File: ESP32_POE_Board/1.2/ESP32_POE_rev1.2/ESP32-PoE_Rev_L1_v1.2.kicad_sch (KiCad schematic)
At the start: 128 parts, among them Q1 Q12MHz/20pF/10ppm/4P/3.2x2.5mm, Q2 BC817-40(SOT23), Q3 BC817-40(SOT23), T1 LMUN2211LT1G(SOT-23), U1 CH340T(SSOP20W), U2 TPS2375D(SO-8), U3 BL4054B-42TPRN(SOT23-5), U4 LAN8710A-EZC(QFN32), U5 TX4138(ESOIC-8), U6 ESP32-WROVER-E, U7 SY8089AAAC(SOT23-5), U8 SN74LVC1G04DBVR(SOT23-5)

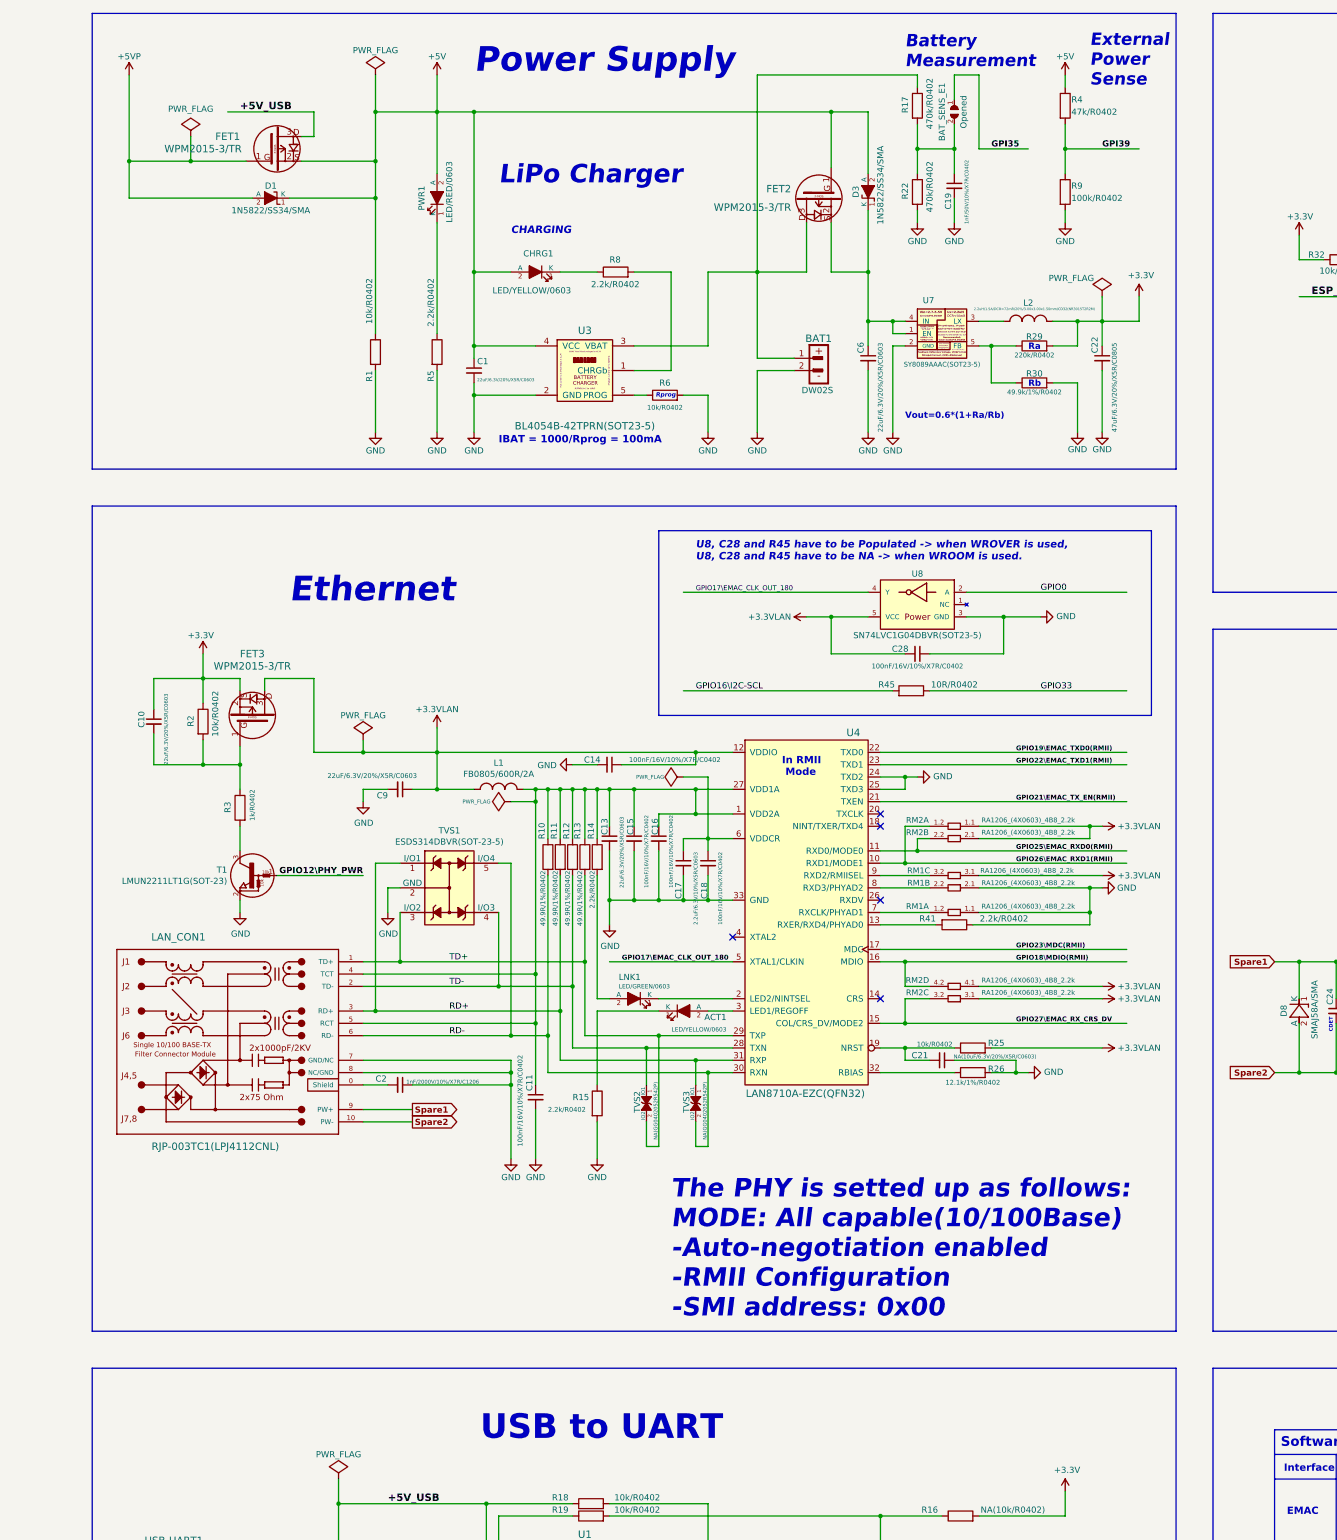
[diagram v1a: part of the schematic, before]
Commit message: new block diagrams
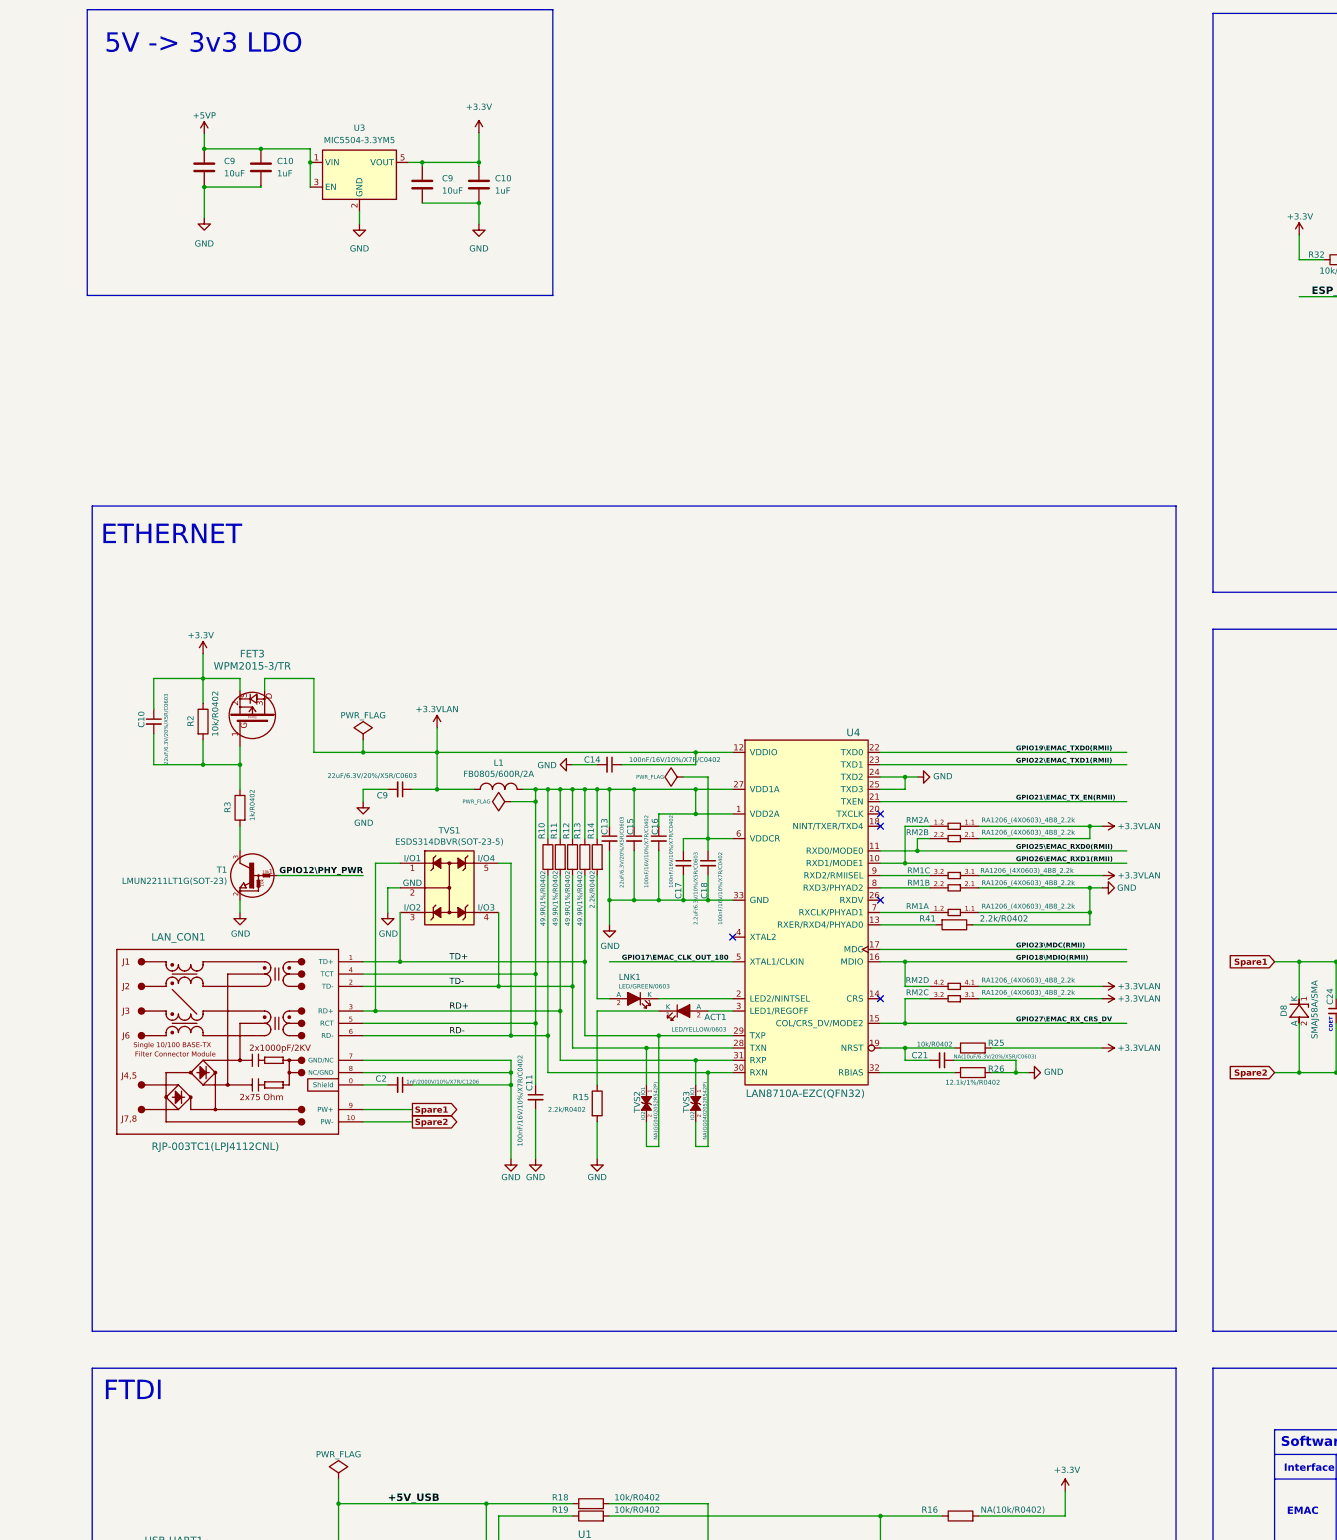
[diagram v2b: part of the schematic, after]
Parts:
- removed BAT1: DW02S, OLIMEX_Connectors-FP:LIPO_BAT_VERTICAL_DW02S, symbol ESP32-PoE_Rev_L1_v1.2-rescue:BAT_CON-ESP32-PoE_Rev_L1
- removed BAT_SENS_E1: Opened, OLIMEX_Jumpers-FP:SJ_1_SMALLER, symbol ESP32-PoE_Rev_L1_v1.2-rescue:SJ-ESP32-PoE_Rev_L1
- removed C1, C6: 22uF/6.3V/20%/X5R/C0603, OLIMEX_RLC-FP:C_0603_5MIL_DWS, symbol ESP32-PoE_Rev_L1_v1.2-rescue:C-ESP32-PoE_Rev_L1
- removed C19: 1nF/50V/10%/X7R/C0402, OLIMEX_RLC-FP:C_0402_5MIL_DWS, symbol ESP32-PoE_Rev_L1_v1.2-rescue:C-ESP32-PoE_Rev_L1
- removed C22: 47uF/6.3V/20%/X5R/C0805, OLIMEX_RLC-FP:C_0805_5MIL_DWS, symbol ESP32-PoE_Rev_L1_v1.2-rescue:C-ESP32-PoE_Rev_L1
- removed C28: 100nF/16V/10%/X7R/C0402, OLIMEX_RLC-FP:C_0402_5MIL_DWS, symbol ESP32-PoE_Rev_L1_v1.2-rescue:C-ESP32-PoE_Rev_L1
- removed CHRG1: LED/YELLOW/0603, OLIMEX_LEDs-FP:LED_0603_KA, symbol ESP32-PoE_Rev_L1_v1.2-rescue:LED-ESP32-PoE_Rev_L1
- removed D1, D3: 1N5822/SS34/SMA, OLIMEX_Diodes-FP:SMA-KA, symbol ESP32-PoE_Rev_L1_v1.2-rescue:D_Schottky-ESP32-PoE_Rev_L1
- removed FET1, FET2: WPM2015-3/TR, OLIMEX_Transistors-FP:SOT23, symbol ESP32-PoE_Rev_L1_v1.2-rescue:P-MOS+DIOD-ESP32-PoE_Rev_L1
- removed L2: 2.2uH/1.5A/DCR=72mR/20%/3.00x3.00x1.50mm/CD32(NR3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, OLIMEX_RLC-FP:CD32, symbol ESP32-PoE_Rev_L1_v1.2-rescue:L-ESP32-PoE_Rev_L1
- removed PWR1: LED/RED/0603, OLIMEX_LEDs-FP:LED_0603_KA, symbol ESP32-PoE_Rev_L1_v1.2-rescue:LED-ESP32-PoE_Rev_L1
- removed R1, R6: 10k/R0402, OLIMEX_RLC-FP:R_0402_5MIL_DWS, symbol ESP32-PoE_Rev_L1_v1.2-rescue:R-ESP32-PoE_Rev_L1
- removed R17, R22: 470k/R0402, OLIMEX_RLC-FP:R_0402_5MIL_DWS, symbol ESP32-PoE_Rev_L1_v1.2-rescue:R-ESP32-PoE_Rev_L1
- removed R29: 220k/R0402, OLIMEX_RLC-FP:R_0402_5MIL_DWS, symbol ESP32-PoE_Rev_L1_v1.2-rescue:R-ESP32-PoE_Rev_L1
- removed R30: 49.9k/1%/R0402, OLIMEX_RLC-FP:R_0402_5MIL_DWS, symbol ESP32-PoE_Rev_L1_v1.2-rescue:R-ESP32-PoE_Rev_L1
- removed R4: 47k/R0402, OLIMEX_RLC-FP:R_0402_5MIL_DWS, symbol ESP32-PoE_Rev_L1_v1.2-rescue:R-ESP32-PoE_Rev_L1
- removed R45: 10R/R0402, OLIMEX_RLC-FP:R_0402_5MIL_DWS, symbol ESP32-PoE_Rev_L1_v1.2-rescue:R-ESP32-PoE_Rev_L1
- removed R5, R8: 2.2k/R0402, OLIMEX_RLC-FP:R_0402_5MIL_DWS, symbol ESP32-PoE_Rev_L1_v1.2-rescue:R-ESP32-PoE_Rev_L1
- removed R9: 100k/R0402, OLIMEX_RLC-FP:R_0402_5MIL_DWS, symbol ESP32-PoE_Rev_L1_v1.2-rescue:R-ESP32-PoE_Rev_L1
- removed U3: BL4054B-42TPRN(SOT23-5), OLIMEX_IC-FP:SOT-23-5, symbol ESP32-PoE_Rev_L1_v1.2-rescue:BL4054B-42TPRN(SOT23-5)-ESP32-PoE_Rev_L1
- removed U7: SY8089AAAC(SOT23-5), OLIMEX_Regulators-FP:SOT-23-5, symbol ESP32-PoE_Rev_L1_v1.2-rescue:SY8009AAAC(SOT23-5)-ESP32-PoE_Rev_L1
- removed U8: SN74LVC1G04DBVR(SOT23-5), OLIMEX_IC-FP:SOT-23-5, symbol ESP32-PoE_Rev_L1_v1.2-rescue:SN74LVC1G04DBVR(SOT23-5)-ESP32-PoE_Rev_L1
- added C10 (x2): 1uF, Capacitor_SMD:C_0201_0603Metric, symbol Device:C
- added C9 (x2): 10uF, Capacitor_SMD:C_0603_1608Metric, symbol Device:C
- added U3: MIC5504-3.3YM5, Package_TO_SOT_SMD:SOT-23-5, symbol Regulator_Linear:MIC5504-3.3YM5
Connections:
- net +3.3V: now also C10.1, C9.1, U3.5 (VOUT)
- net +5VP: now also C10.1, C9.1, U3.1 (VIN), U3.3 (EN)
- net GND: now also C10.2, C10.2, C9.2, C9.2, U3.2 (GND)
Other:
- note added: "5V -> 3v3 LDO"
- note added: "ETHERNET"
- note added: "FTDI"
- note removed: "Battery Measurement"
- note removed: "CHARGING"
- note removed: "Ethernet"
- note removed: "External Power Sense"
- note removed: "IBAT = 1000/Rprog = 100mA"
- note removed: "In RMII Mode"
- note removed: "LiPo Charger"
- note removed: "Power Supply"
- note removed: "Rprog"
- note removed: "The PHY is setted up as follows: MODE: All capable(10/100Base) -Auto-negotiation enabled -RMII Configuration -SMI address: 0x00"
- note removed: "U8, C28 and R45 have to be Populated -> when WROVER is used, U8, C28 and R45 have to be NA -> when WROOM is used."
- note removed: "USB to UART"
- note removed: "Vout=0.6*(1+Ra/Rb)"

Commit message: fixing POE board symbols + circuit
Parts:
- removed C3: 47uF/6.3V/20%/X5R/C0805, OLIMEX_RLC-FP:C_0805_5MIL_DWS, symbol ESP32-PoE_Rev_L1_v1.2-rescue:C-ESP32-PoE_Rev_L1
- removed EXT1, EXT2: NS(HN1x10), OLIMEX_Connectors-FP:HN1x10, symbol ESP32-PoE_Rev_L1_v1.2-rescue:CON10-ESP32-PoE_Rev_L1
- removed L5: FB0805/600R/2A, OLIMEX_RLC-FP:L_0805_5MIL_DWS, symbol ESP32-PoE_Rev_L1_v1.2-rescue:L-ESP32-PoE_Rev_L1
- removed MICRO_SD1: TFC-9P-1.7H(ATFFS150A01BR016), OLIMEX_Connectors-FP:uSD(TFC-9P-1.xH(ATFFS150A01BR016)), symbol ESP32-PoE_Rev_L1_v1.2-rescue:MICRO_SD(TFC-9P-1.xH(ATFFS150A01BR016))-ESP32-PoE_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
- removed R39: 10k/R0402, OLIMEX_RLC-FP:R_0402_5MIL_DWS, symbol ESP32-PoE_Rev_L1_v1.2-rescue:R-ESP32-PoE_Rev_L1
- removed R40: 10R/R0402, OLIMEX_RLC-FP:R_0402_5MIL_DWS, symbol ESP32-PoE_Rev_L1_v1.2-rescue:R-ESP32-PoE_Rev_L1
- removed R46: 220R/R0402, OLIMEX_RLC-FP:R_0402_5MIL_DWS, symbol ESP32-PoE_Rev_L1_v1.2-rescue:R-ESP32-PoE_Rev_L1
- removed RM3: RA1206_(4X0603)_4B8_2.2k, OLIMEX_RLC-FP:R_MATRIX_4, symbol ESP32-PoE_Rev_L1_v1.2-rescue:RA1206_(4x0603)_4B8_Smashed-ESP32-PoE_Rev_L1
- added C10: 1uF, Capacitor_SMD:C_0201_0603Metric, symbol Device:C
- added C17: 100nF, Capacitor_SMD:C_0402_1005Metric, symbol Device:C
- added C17: 1nF, Capacitor_SMD:C_1206_3216Metric, symbol Device:C
- added C9: 10uF, Capacitor_SMD:C_0603_1608Metric, symbol Device:C
- added D1, D11, D3: 1N5819, Diode_THT:D_DO-41_SOD81_P10.16mm_Horizontal, symbol Diode:1N5819
- added D10: BAT54C, Package_TO_SOT_SMD:SOT-23, symbol Diode:BAT54C
- added FB1: 600R-2A, Capacitor_SMD:C_0805_2012Metric, symbol Device:FerriteBead
- added J1: USB_C_Receptacle, Connector_USB:USB_C_Receptacle_Molex_105450-0101-L, symbol Connector:USB_C_Receptacle
- added J2: SI-46020-F, SI-46020-F:BEL_SI-46020-F, symbol SI-46020-F:SI-46020-F
- added Q4, Q5: BC817, Package_TO_SOT_SMD:SOT-23, symbol Transistor_BJT:BC817
- added R14: 220, Resistor_SMD:R_0402_1005Metric, symbol Device:R_US
- added R14 (x2): 1k, Resistor_SMD:R_0402_1005Metric, symbol Device:R_US
- added U4: FT232RQ, FT232RQ:QFN50P500X500X90-33N, symbol FT232RQ:FT232RQ
- added U7: ESDS314DBVR, DBV0005A_N, symbol ESDS314DBVR:ESDS314DBVR
- added U9: LAN8710A-EZC, QFN32_5X5MC_MCH, symbol LAN8710A_EZC:LAN8710A-EZC
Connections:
- net +5V: now also C10.1, C9.1, FB1.1, J1.A1 (GND), J1.A12 (GND), J1.A4 (VBUS), J1.A9 (VBUS), J1.B1 (GND), J1.B12 (GND), J1.B4 (VBUS), J1.B9 (VBUS), J1.S1 (SHIELD), U4.1 (VCCIO), U4.19 (VCC)
- net ESP_EN: now also D11.2 (A)
- net GND: now also C10.2, C17.1, C9.2, FB1.2, J2.7 (P7)
- net GPIO0: now also D10.1
- net GPIO2\HS2_DATA0: now also D10.2
- new net: D3.2 (A), U4.2 (RXD)
- new net: D1.1 (K), U4.30 (TXD)
- new net: J1.A6 (D+), J1.B6 (D+), U4.14 (USBDP)
- new net: J1.A7 (D-), J1.B7 (D-), U4.15 (USBDM)
- new net: Q5.2 (E), R14.1
- new net: D10.3, R14.2
- new net: Q5.3 (C), R14.1, U4.31 (~{DTR})
- new net: Q4.1 (B), R14.2
- new net: Q4.2 (E), R14.1, U4.32 (~{RTS})
- new net: Q5.1 (B), R14.2
- new net: D11.1 (K), Q4.3 (C)
- new net: U4.17 (GND), U4.20 (GND), U4.4 (GND)
- new net: C17.2, J2.S1 (SHIELD), J2.S2 (SHIELD)
- new net GPIO1_U0TXD: D3.1 (K)
- new net GPIO3_U0RXD: D1.2 (A)
- new net PW+: J2.9 (P9)
- new net PW-: J2.10 (P10)
- no-connect marks 22 -> 19
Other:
- note removed: "SD/MMC Card"

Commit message: updates
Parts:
- added SW1 (x2): PTS815 SJM 250 SMTR LFS, SW4_PTS815 SJM 250 SMTR LFS_CNK, symbol PTS815:PTS815_SJM_250_SMTR_LFS
- added U10: ESP32-WROOM-32, RF_Module:ESP32-WROOM-32, symbol RF_Module:ESP32-WROOM-32
- added U11: TPS2375D, D8, symbol TPS2375D:TPS2375D
- added U12: LM5145RGYR, RGY0020B, symbol LM5145RGYR:LM5145RGYR
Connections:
- net at J2.1 (TD+): now also U7.1 (I_O1)
- net at J2.3 (TD-): now also U7.4 (I_O3)
- net at J2.4 (RD+): now also U7.3 (I_O2)
- net at J2.6 (RD-): now also U7.5 (I_O4)
- new net: U10.1 (GND), U10.15 (GND), U10.38 (GND), U10.39 (GND)
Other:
- moved on the sheet: C17, J2, U7, U9

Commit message: fixing ethernet and poe power circuits
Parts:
- removed U12: LM5145RGYR, RGY0020B, symbol LM5145RGYR:LM5145RGYR
- added C36: C_Polarized, symbol Device:C_Polarized
- added C9: 2.2uF, Capacitor_SMD:C_0402_1005Metric, symbol Device:C
- added C9: 22uF, Capacitor_SMD:C_0603_1608Metric, symbol Device:C
- added C9 (x3): 100nF, Capacitor_SMD:C_0402_1005Metric, symbol Device:C
- added D14: SMAJ58A, Diode_SMD:D_SMA, symbol Diode:SMAJ58A
- added D5 (x2): LED, LED_SMD:LED_0603_1608Metric, symbol Device:LED
- added R14: 130k, Resistor_SMD:R_0402_1005Metric, symbol Device:R_US
- added R14 (x4): 2.2k, Resistor_SMD:R_0402_1005Metric, symbol Device:R_US
- added R14: 24.9k, Resistor_SMD:R_0402_1005Metric, symbol Device:R_US
- added R14: 24.9k, Resistor_SMD:R_1206_3216Metric, symbol Device:R_US
- added R14: 4.42k, Resistor_SMD:R_0402_1005Metric, symbol Device:R_US
- added R14 (x2): 10k, Resistor_SMD:R_0402_1005Metric, symbol Device:R_US
- added R14: 4.7k, Resistor_SMD:R_2512_6332Metric, symbol Device:R_US
- added U12: TX4138, ESOIC8_XDS, symbol TX4138:TX4138
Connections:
- net +5V: now also C17.2, J2.2 (TCT), J2.5 (RCT), U9.1 (VDD2A), U9.12 (VDDIO), U9.27 (VDD1A), U9.6 (VDDCR), C9.1, C9.1, C9.1, C9.1, R14.1, R14.1, R14.2
- net GND: now also C17.1, U11.5 (RTN), U7.2 (GND), C36.2, C9.2, C9.2, C9.2, C9.2, R14.1, R14.2
- net PW+: now also C9.1, D14.1 (A1), R14.1, R14.1
- net PW-: now also U11.4 (VSS), C9.2, D14.2 (A2), R14.1, R14.1, R14.2
- net RD+: now also J2.4 (RD+), U7.3 (I_O2)
- net RD-: now also J2.6 (RD-), U7.5 (I_O4)
- net TD+: now also J2.1 (TD+), U7.1 (I_O1)
- net TD-: now also J2.3 (TD-), U7.4 (I_O3)
- net at U11.1 (ILIM): now also R14.2
- net at U11.2 (CLASS): now also R14.2
- net at U11.3 (DET): now also U11.8 (VDD), C36.1, R14.1, R14.2, R14.2
- net at U11.6 (PG): now also U12.6 (EN)
- net at U11.7 (NC): now also R14.1, R14.2
- net GPIO27/EMAC_RX_CRS_DV: now reaches U9.15 (COL/CRS_DV/*MODE2)
- net GPIO27/EMAC_RX_CRS_DV: now also R14.2
- net GPIO18/MDIO(RMII): now reaches U9.16 (MDIO)
- net GPIO18/MDIO(RMII): now also R14.2
- net at U9.2 (LED2/*NINTSEL): now also D5.1 (K)
- net at U9.3 (LED1/*REGOFF): now also D5.2 (A)
- net GPIO17/EMAC_CLK_OUT_180: now reaches U9.5 (XTAL1/CLKIN)
- new net: D5.1 (K), R14.1
- new net: D5.2 (A), R14.1
- new net: R14.2, U12.EPAD (ILIM)
- no-connect marks 19 -> 22
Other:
- moved on the sheet: C17, J2, U7, U9

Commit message: updates
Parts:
- added C10: 1uF, Capacitor_SMD:C_0201_0603Metric, symbol Device:C
- added C39: C_Polarized, symbol Device:C_Polarized
- added C9: 100nF, Capacitor_SMD:C_0402_1005Metric, symbol Device:C
- added C9: 12pF, Capacitor_SMD:C_0402_1005Metric, symbol Device:C
- added D15: D_Schottky, symbol Device:D_Schottky
- added L2: ASPI-0804T-330M-T, ASPI-0804T-330M-T:IND_ASPI-0804T-330M-T, symbol ASPI-0804T-330M-T:ASPI-0804T-330M-T
- added R14: 30.1k, Resistor_SMD:R_0402_1005Metric, symbol Device:R_US
- added R14: 10k, Resistor_SMD:R_0402_1005Metric, symbol Device:R_US
- added R14: 5.23k, Resistor_SMD:R_0402_1005Metric, symbol Device:R_US
- added R14: 4.7, Resistor_SMD:R_0402_1005Metric, symbol Device:R_US
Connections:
- net +3.3V: now also U10.2 (VDD), R14.2
- net +5V: now also C39.1, C9.1, L2.2, R14.2
- net ESP_EN: now also U10.3 (EN), C10.1, R14.1
- net GND: now also U10.1 (GND), U10.15 (GND), U10.38 (GND), U10.39 (GND), U12.4 (GND), C10.2, C39.2, D15.2 (A), R14.1
- net at C36.1, R14.1, R14.2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: now also U12.3 (VIN)
- net at R14.2, U12.EPAD (ILIM): now also U12.2 (ILIM)
- net at U12.1 (SW): now also C9.2, D15.1 (K), L2.1
- net at U12.5 (FB): now also C9.2, R14.1, R14.2
- net at U12.8 (BS): now also R14.2
- new net: C9.1, R14.1
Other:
- note added: "Ethernet POE + 5V Buck"
- note added: "Schottky needs to be picked, D5"
- note added: "What value for polarized cap"
- moved on the sheet: C10, C12, C23, C24, C25, C26, C27, C36, C4, C5, C7, C8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

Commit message: finished ESP for POE board
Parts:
- removed BUT1, RST1: IT1185AU2, OLIMEX_Buttons-FP:IT1185AU2_V2, symbol ESP32-PoE_Rev_L1_v1.2-rescue:SIDE_WTCM-TR(3x4)-ESP32-PoE_Rev_L1
- removed R47: 220R/R0402, OLIMEX_RLC-FP:R_0402_5MIL_DWS, symbol ESP32-PoE_Rev_L1_v1.2-rescue:R-ESP32-PoE_Rev_L1
- removed R48: 10k/R0402, OLIMEX_RLC-FP:R_0402_5MIL_DWS, symbol ESP32-PoE_Rev_L1_v1.2-rescue:R-ESP32-PoE_Rev_L1
- removed R49: NA/R0402, OLIMEX_RLC-FP:R_0402_5MIL_DWS, symbol ESP32-PoE_Rev_L1_v1.2-rescue:R-ESP32-PoE_Rev_L1
- added R14: 10k, Resistor_SMD:R_0402_1005Metric, symbol Device:R_US
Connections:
- net +3.3V: now also R14.2
- net ESP_EN: now also SW1.1
- net GND: now also SW1.4, SW1.4
- net GPI34\BUT1: now also SW1.1, U10.6 (IO34)
- net GPI35: now also U10.7 (IO35)
- net GPI36\U1RXD: now also U10.4 (SENSOR_VP)
- net GPI39: now also U10.5 (SENSOR_VN)
- net GPIO0: now also U10.25 (IO0)
- net GPIO12\PHY_PWR: now also U10.14 (IO12)
- net GPIO13\I2C-SDA: now also U10.16 (IO13)
- net GPIO14\HS2_CLK: now also U10.13 (IO14)
- net GPIO15\HS2_CMD: now also U10.23 (IO15)
- net GPIO16\I2C-SCL: now also U10.27 (IO16)
- net GPIO17\EMAC_CLK_OUT_180: now also U10.28 (IO17)
- net GPIO18\MDIO(RMII): now also U10.30 (IO18)
- net GPIO19\EMAC_TXD0(RMII): now also U10.31 (IO19)
- net GPIO1\U0TXD: now also U10.35 (TXD0/IO1)
- net GPIO21\EMAC_TX_EN(RMII): now also U10.33 (IO21)
- net GPIO22\EMAC_TXD1(RMII): now also U10.36 (IO22)
- net GPIO23\MDC(RMII): now also U10.37 (IO23)
- net GPIO25\EMAC_RXD0(RMII): now also U10.10 (IO25)
- net GPIO26\EMAC_RXD1(RMII): now also U10.11 (IO26)
- net GPIO27\EMAC_RX_CRS_DV: now also U10.12 (IO27)
- net GPIO2\HS2_DATA0: now also U10.24 (IO2)
- net GPIO32: now also U10.8 (IO32)
- net GPIO33: now also U10.9 (IO33)
- net GPIO3\U0RXD: now also U10.34 (RXD0/IO3)
- net GPIO4\U1TXD: now also U10.26 (IO4)
- net GPIO5\SPI_CS: now also U10.29 (IO5)
- net at SW1.2: now also R14.1
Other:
- note added: "ESP32"
- moved on the sheet: C10, C20, R14, R32, R44, SW1, U10, U6
